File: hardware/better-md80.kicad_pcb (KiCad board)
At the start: 4 copper layers, 56.7 x 54.7 mm, 145 parts, among them J1 Micro-Fit 2x3, J10 Phase A, J11 Phase B, J12 Phase C, J2 Micro-Fit 2x3, J3 AUX1 SPI enc, J4 AUX2 RS422, J5 Motor NTC, J6 TC2030-NL, K1 CPC1017N, Q1 ISC022N10NM6, Q2 ISC022N10NM6, Q3 ISC022N10NM6, Q4 ISC022N10NM6, Q5 ISC022N10NM6, Q6 ISC022N10NM6, U1 LM5164DDAR, U2 TPS62163DSGR, U3 TLV75533PDBVR, U4 DRV8353SRTAR, U5 STM32G474CEU6, U6 TCAN1044AVDR, U7 AS5047P-ATSM, U8 MAX3490EESA+, Y1 8MHz

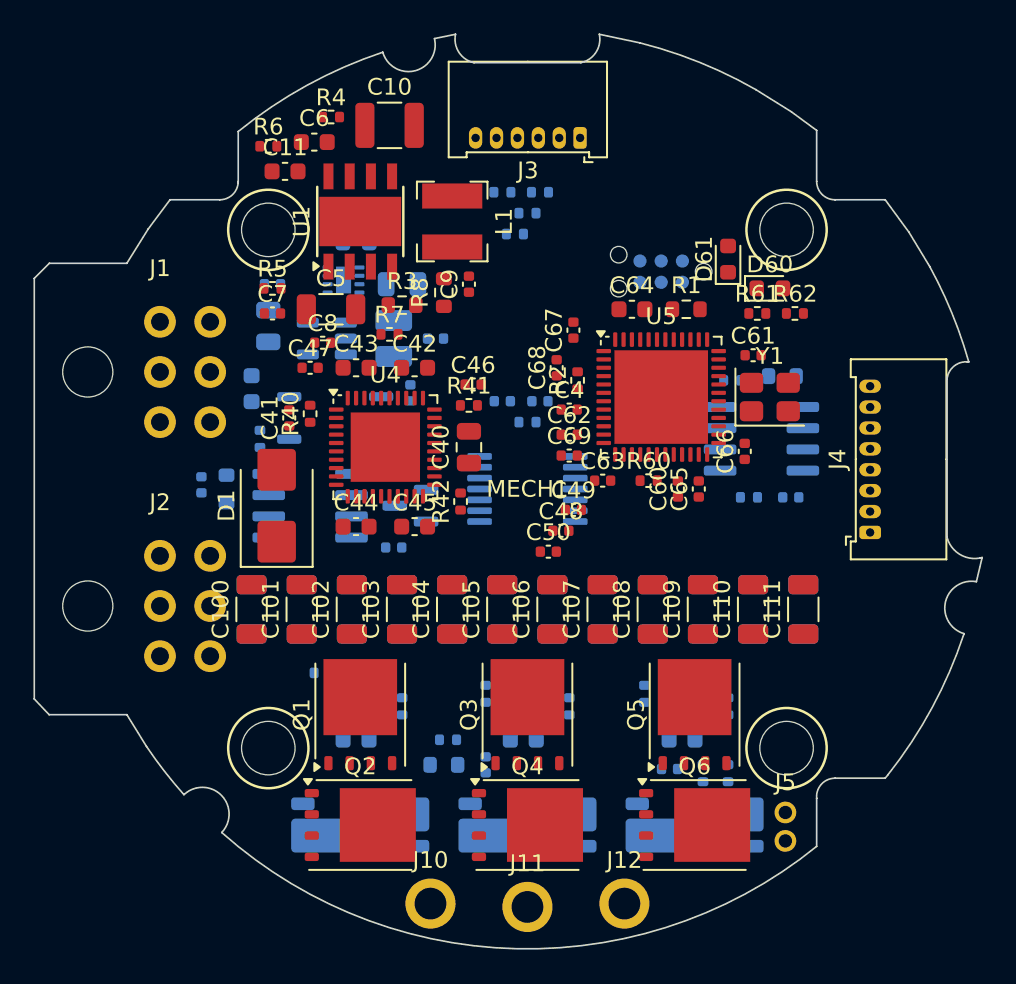
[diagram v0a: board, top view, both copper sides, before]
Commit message: Route the board: KiCad 10, 6 layers, pours, fan-out, silkscreen clean-up
Autorouted with Freerouting after QFN fan-out; remaining nets routed with
tools/hand_route.py. DRC: 0 unconnected, only the MD80-inherent AUX1/screw
courtyard overlap. GND plane on In1 still carries signal tracks (next pass).

Co-Authored-By: Claude Opus 5.5 (1M context) <noreply@anthropic.com>
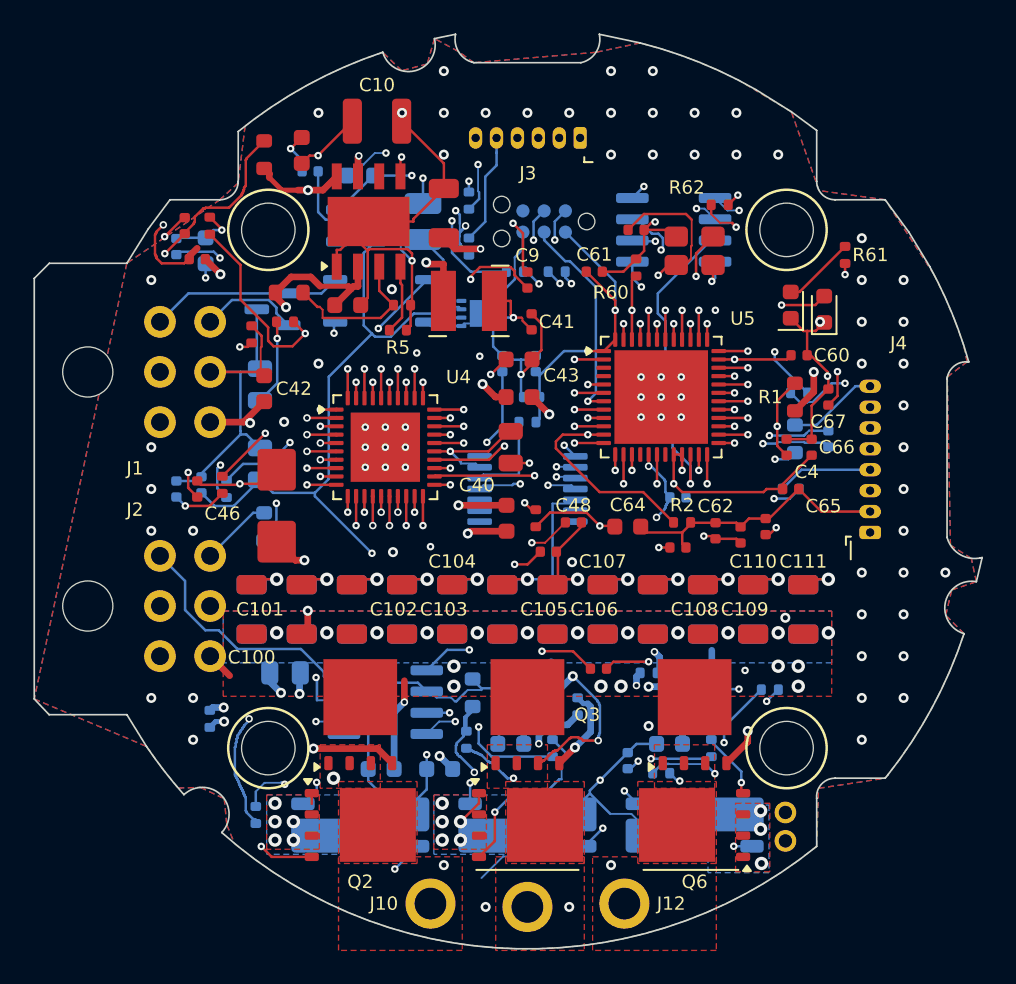
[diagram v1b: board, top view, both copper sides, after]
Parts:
- moved C32 19.7 mm to (159.0, 100.5), turned to 0 degrees
- moved C47 18.0 mm to (151.2, 103.8)
- moved C46 17.6 mm to (130.2, 100.0), turned to 90 degrees
- moved C16 16.5 mm to (129.0, 85.5)
- moved R42 16.0 mm to (133.5, 90.8)
- moved C67 15.8 mm to (168.0, 94.5)
- moved C41 15.6 mm to (150.2, 90.0)
- moved D70 14.4 mm to (134.8, 89.2)
- moved C13 13.7 mm to (134.0, 98.5), turned to 90 degrees
- moved U8 13.6 mm to (158.8, 84.5)
- moved R8 13.6 mm to (134.2, 80.0)
- moved C4 13.2 mm to (165.5, 97.5), turned to 90 degrees
- moved C64 13.0 mm to (156.0, 102.2)
- moved R60 12.8 mm to (156.5, 86.8), turned to 90 degrees
- moved U6 12.6 mm to (141.5, 112.8)
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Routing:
- net GND: track 0.00 -> 241.3 mm, vias 0 -> 99
- net +3V3: track 0.00 -> 159.2 mm, vias 0 -> 13
- net +3V3A: track 0.00 -> 116.7 mm, vias 0 -> 9
- net VBUS: track 0.00 -> 112.5 mm, vias 0 -> 32
- net +5V: track 0.00 -> 102.2 mm, vias 0 -> 3
- net +12V: track 0.00 -> 68.9 mm, vias 0 -> 6
- net SPI3_MOSI: track 0.00 -> 46.6 mm, vias 0 -> 4
- net TEMP_FET: track 0.00 -> 43.9 mm, vias 0 -> 3
- net CANH: track 0.00 -> 42.1 mm
- net DRV_nFAULT: track 0.00 -> 40.7 mm, vias 0 -> 4
- net CAN_RX: track 0.00 -> 39.8 mm, vias 0 -> 3
- net CAN_TERM_EN: track 0.00 -> 39.0 mm, vias 0 -> 2
- net CANL: track 0.00 -> 38.8 mm, vias 0 -> 1
- net CAN_TX: track 0.00 -> 37.6 mm, vias 0 -> 2
- net FB12: track 0.00 -> 37.2 mm, vias 0 -> 3
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- added copper zone on B.Cu, net GND
- added copper zone on F.Cu, net GND
- added copper zone on In1.Cu, net GND
- added copper zone on In2.Cu, net GND
- added copper zone on In3.Cu, net GND
- added copper zone on In4.Cu, net GND
- added copper zone on B.Cu, net LSA
- added copper zone on F.Cu, net LSA
- added copper zone on B.Cu, net LSB
- added copper zone on F.Cu, net LSB
- added copper zone on B.Cu, net LSC
- added copper zone on F.Cu, net LSC
- added copper zone on F.Cu, net PHA
- added copper zone on In4.Cu, net PHA
- added copper zone on F.Cu, net PHB
- added copper zone on In4.Cu, net PHB
- added copper zone on F.Cu, net PHC
- added copper zone on In4.Cu, net PHC
- added copper zone on B.Cu, net VBUS
- added copper zone on F.Cu, net VBUS
- added copper zone on In4.Cu, net VBUS
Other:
- copper layers 4 -> 6

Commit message: Re-route with a solid In1 GND plane; add simulations
Freerouting re-run with In1 locked as a power plane (0 signal tracks on In1),
leftovers routed with tools/hand_route.py. DRC: 0 unconnected, only the
MD80-inherent AUX1/screw courtyard overlap.

sim/: FastHenry loop inductance (5.0 nH), LTspice double pulse and bus
surge/regen, MATLAB current loop. Findings and recommended changes in
docs/simulation.md.

Co-Authored-By: Claude Opus 5.5 (1M context) <noreply@anthropic.com>
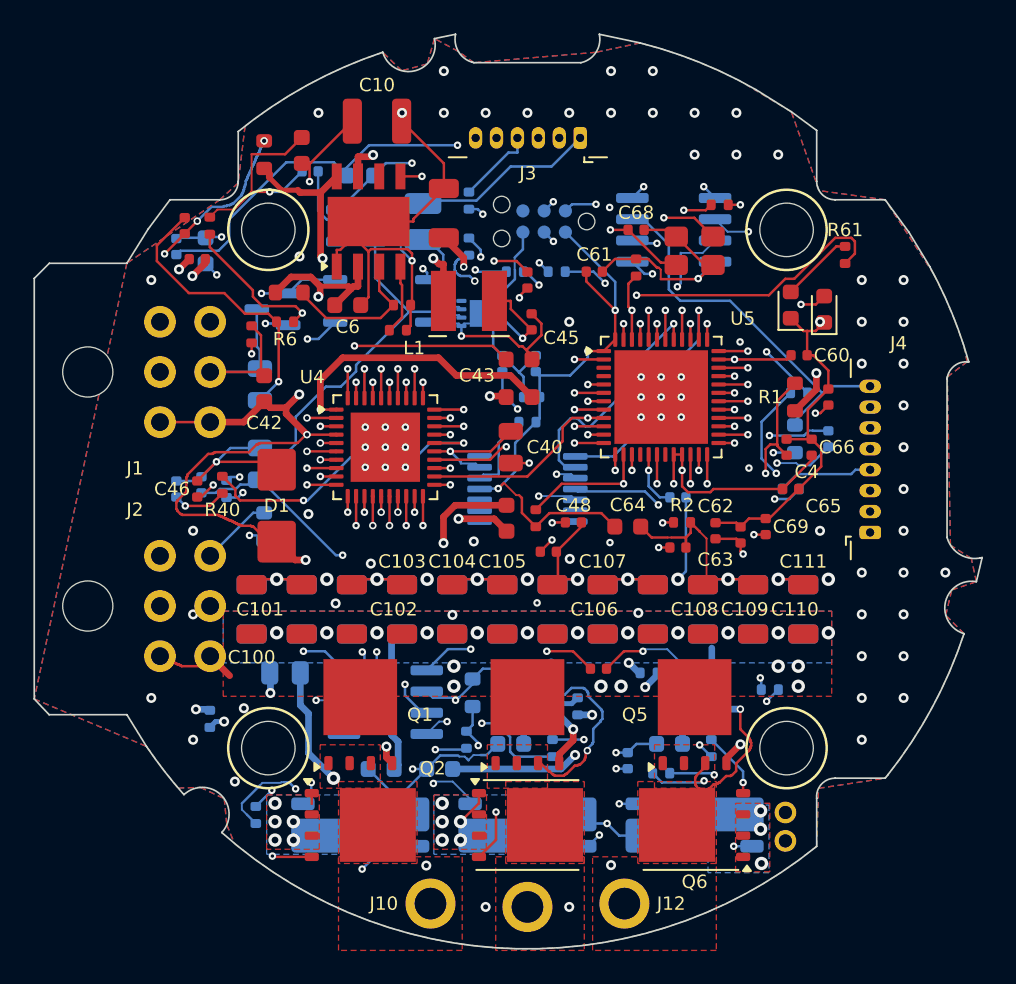
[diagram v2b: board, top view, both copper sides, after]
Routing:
- net TEMP_FET: track 43.9 -> 27.0 mm, vias 3 -> 2
- net INHA: track 24.4 -> 40.4 mm
- net DRV_EN: track 36.8 -> 51.7 mm
- net SNUBA: track 13.8 -> 28.7 mm
- net BST12: track 32.7 -> 18.6 mm, vias 2 -> 3
- net SPI3_MOSI: track 46.6 -> 34.2 mm, vias 4 -> 3
- net CANH: track 42.1 -> 53.6 mm, vias 0 -> 2
- net CAN_TX: track 37.6 -> 48.1 mm
- net DRV_nFAULT: track 40.7 -> 50.7 mm, vias 4 -> 3
- net PHB: track 29.1 -> 39.0 mm, vias 4 -> 5
- net PHC: track 29.2 -> 38.2 mm, vias 3 -> 5
- net INLC: track 26.7 -> 35.0 mm, vias 2 -> 4
- net FB12: track 37.2 -> 30.5 mm
- net PHA: track 23.5 -> 29.7 mm
- net TERM_LED: track 17.9 -> 23.8 mm
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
